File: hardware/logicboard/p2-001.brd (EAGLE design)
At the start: 72 x 72 mm, 49 parts, among them IC1 4066N, IC2 LTC485N, IC3 74LS07N, J1 LED, J2 RLY, J3 PWR, J4 DC9V, J5 Display, K1 G5V1, T1 2SC1815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

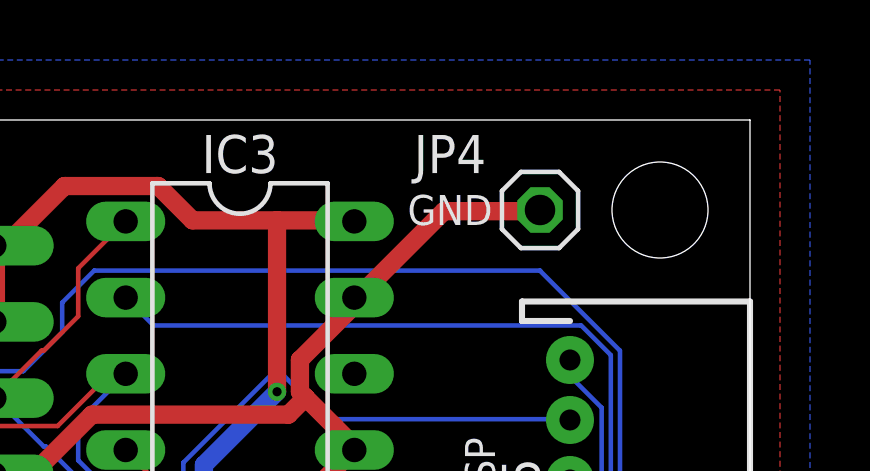
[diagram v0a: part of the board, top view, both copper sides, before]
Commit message: Renumbered number of jumpers.
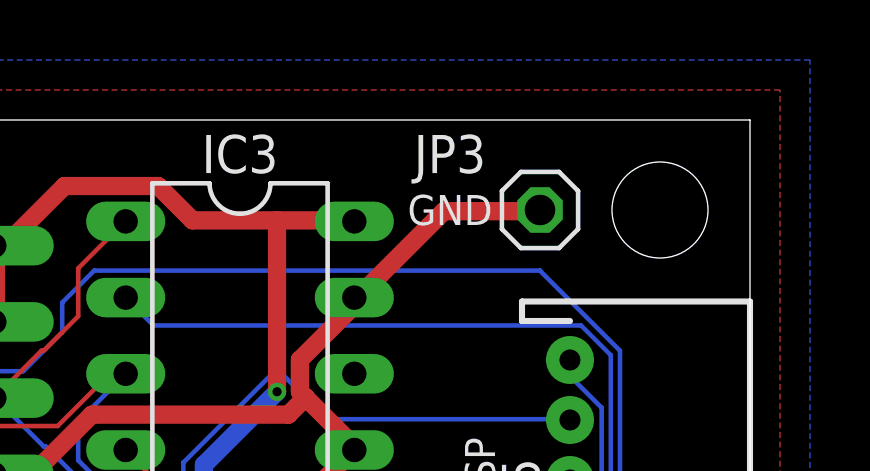
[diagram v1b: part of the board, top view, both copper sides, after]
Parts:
- renumbered JP4 to JP3
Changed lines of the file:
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@@
 <?xml version="1.0" encoding="utf-8"?>
 <!DOCTYPE eagle SYSTEM "eagle.dtd">
-<eagle version="9.5.2">
+<eagle version="9.6.1">
 <drawing>
 <settings>
@@
 <attribute name="VALUE" x="18" y="21" size="0.8128" layer="27" ratio="10" rot="R90" align="bottom-center"/>
 </element>
-<element name="JP4" library="pinhead" library_urn="urn:adsk.eagle:library:325" package="1X01" package3d_urn="urn:adsk.eagle:package:22485/2" value="GNDPIN" x="65" y="69" smashed="yes">
+<element name="JP3" library="pinhead" library_urn="urn:adsk.eagle:library:325" package="1X01" package3d_urn="urn:adsk.eagle:package:22485/2" value="GNDPIN" x="65" y="69" smashed="yes">
 <attribute name="NAME" x="62" y="71.5" size="1.27" layer="25" ratio="10" align="top-center"/>
 <attribute name="POPULARITY" value="64" x="65" y="69" size="1.778" layer="27" display="off"/>
@@
 <contactref element="IC2" pad="5"/>
 <contactref element="OK1" pad="5"/>
-<contactref element="JP4" pad="1"/>
+<contactref element="JP3" pad="1"/>
 <contactref element="C1" pad="2"/>
 <contactref element="C3" pad="2"/>

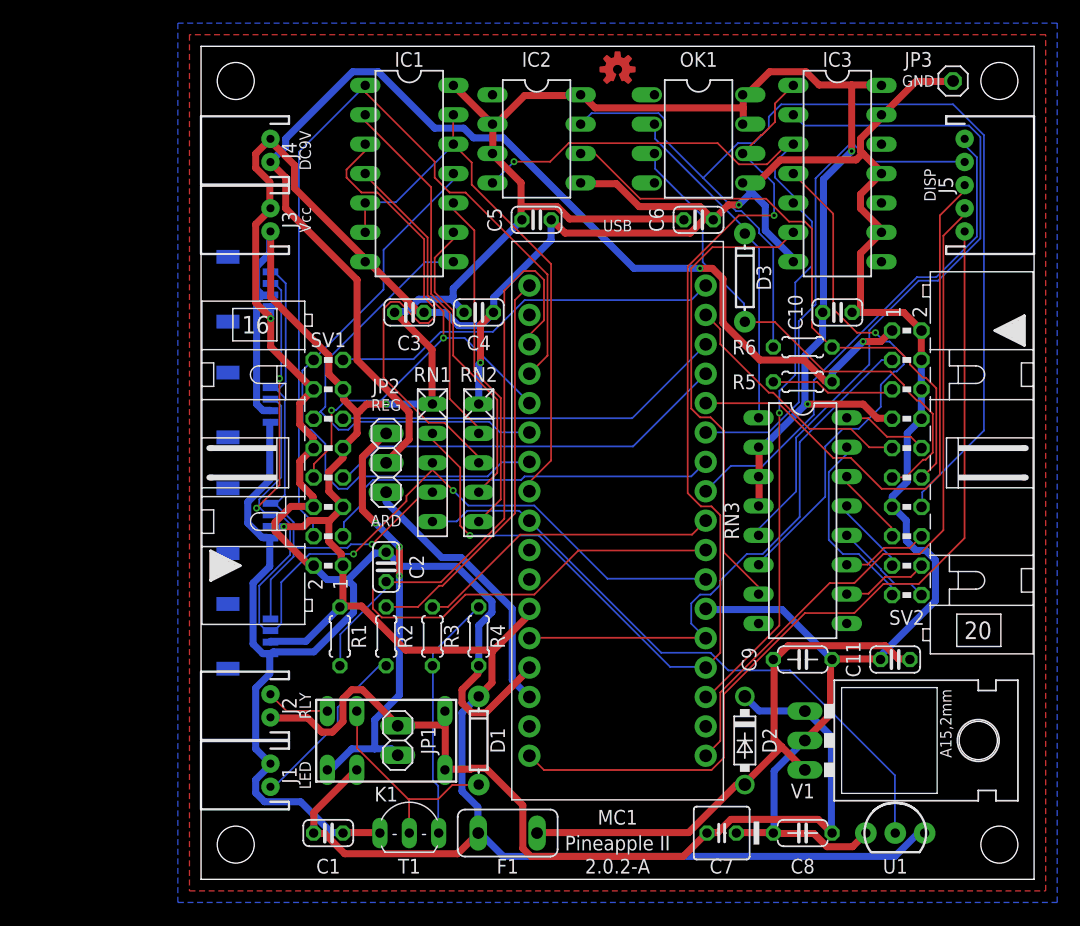
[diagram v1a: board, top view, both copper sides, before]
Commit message: Now Vcc is directly connected to the regulator.
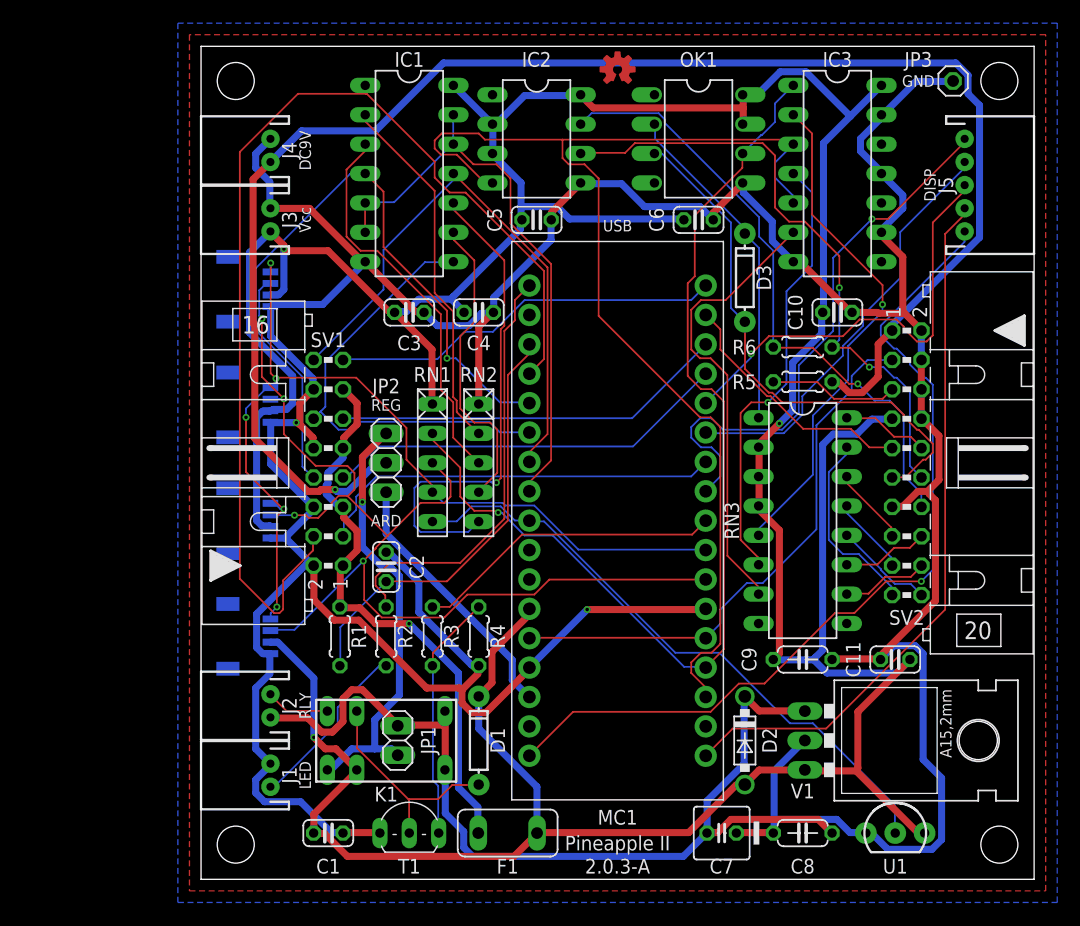
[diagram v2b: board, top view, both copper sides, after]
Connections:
- net +5V: now also F1.1, R1.2, SV1.1, SV1.13, SV1.5, SV1.9; no longer C11.1, C9.1, D2.A, F1.2, V1.OUT
- net VCC: now also C11.1, C9.1, D2.A, F1.2, V1.OUT; no longer F1.1, R1.2, SV1.1, SV1.13, SV1.5, SV1.9
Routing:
- net MTX-: track 94.7 -> 53.7 mm, vias 0 -> 1
- net VCC: track 317.0 -> 350.9 mm, vias 4 -> 3
- net +9V: track 104.8 -> 138.3 mm, vias 2 -> 1
- net ANLG1: track 74.8 -> 95.1 mm
- net TX: track 82.6 -> 102.2 mm, vias 2 -> 0
- net MTH: track 60.3 -> 44.0 mm, vias 0 -> 1
- net ANLG2: track 45.5 -> 60.7 mm, vias 2 -> 1
- net AREF: track 51.8 -> 37.6 mm
- net N$2: track 30.0 -> 43.1 mm, vias 0 -> 1
- net DISP3: track 49.7 -> 38.0 mm, vias 0 -> 1
- net ANLG2PDN: track 42.8 -> 33.8 mm
- net DISP2: track 43.8 -> 36.7 mm
- net MO1: track 45.1 -> 38.5 mm
- net DISP1: track 43.2 -> 48.7 mm, vias 0 -> 1
- net RX: track 95.8 -> 90.4 mm, vias 2 -> 1
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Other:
- board text added: "2.0.3-A"
- board text removed: "2.0.2-A"

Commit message: Changed resistance attached to LED.
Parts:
- R2: value 160 -> 120
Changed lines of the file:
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@@
 <?xml version="1.0" encoding="utf-8"?>
 <!DOCTYPE eagle SYSTEM "eagle.dtd">
-<eagle version="9.6.1">
+<eagle version="9.5.2">
 <drawing>
 <settings>
@@
 <attribute name="VALUE" x="69" y="60" size="0.8128" layer="27" ratio="20" rot="R90" align="bottom-center"/>
 </element>
-<element name="R2" library="resistor" library_urn="urn:adsk.eagle:library:348" package="0204/5" package3d_urn="urn:adsk.eagle:package:23488/1" value="160" x="16" y="21" smashed="yes" rot="R90">
+<element name="R2" library="resistor" library_urn="urn:adsk.eagle:library:348" package="0204/5" package3d_urn="urn:adsk.eagle:package:23488/1" value="120" x="16" y="21" smashed="yes" rot="R90">
 <attribute name="NAME" x="17" y="21" size="1.27" layer="25" ratio="10" rot="R90" align="top-center"/>
 <attribute name="VALUE" x="18" y="21" size="0.8128" layer="27" ratio="10" rot="R90" align="bottom-center"/>

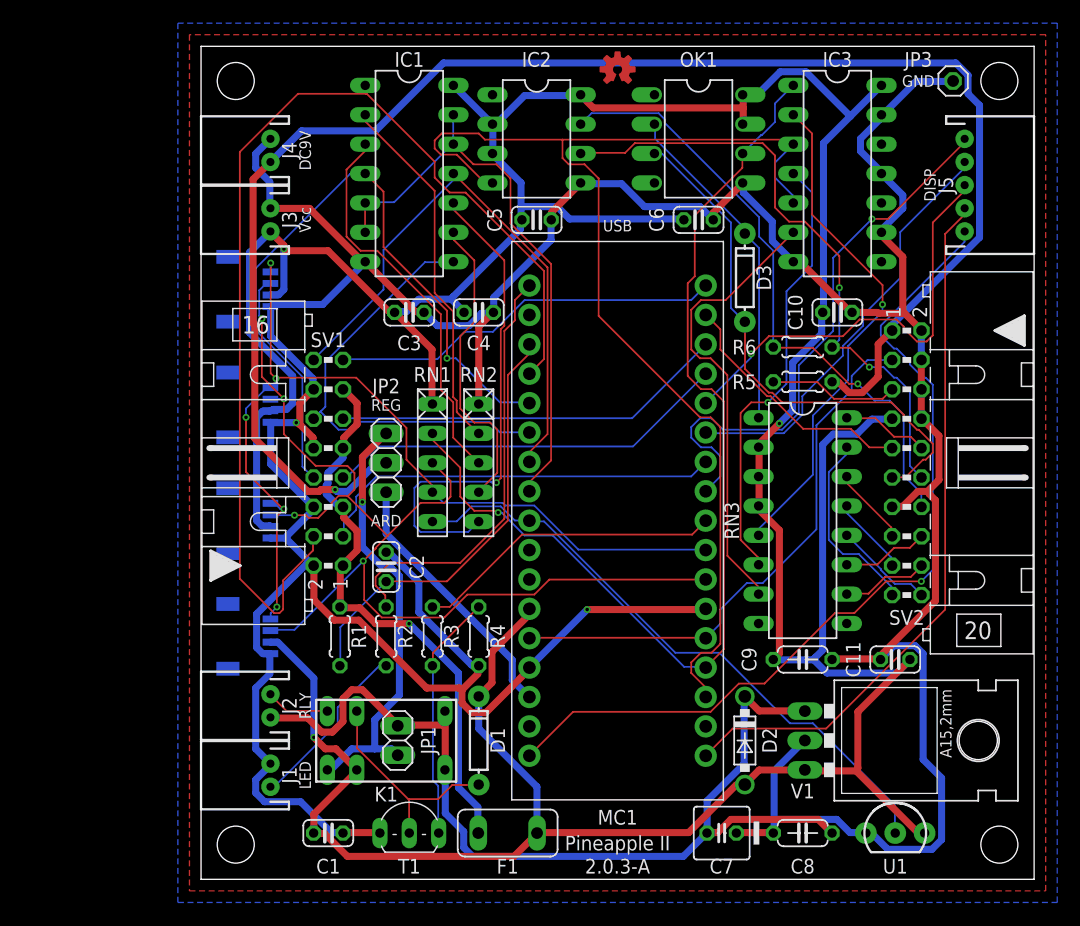
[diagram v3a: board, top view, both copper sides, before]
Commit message: Changed position of capacitors.
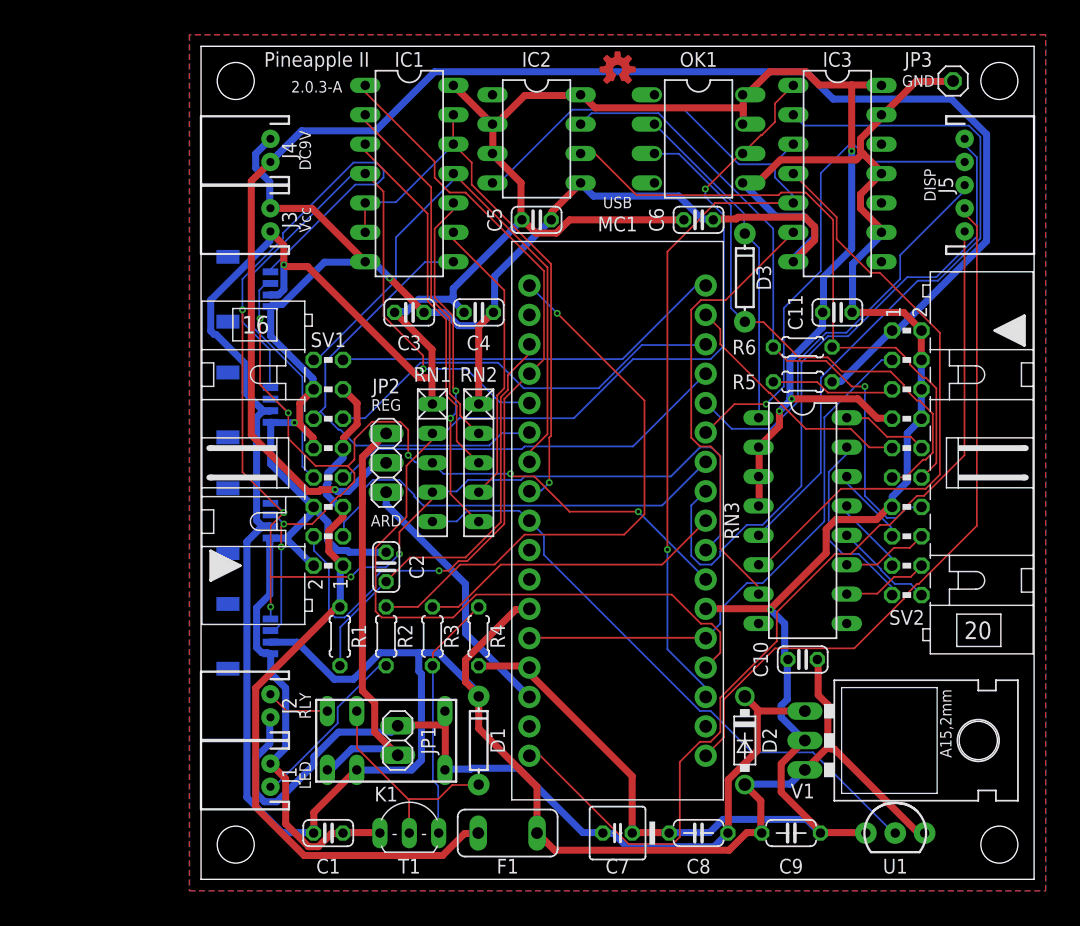
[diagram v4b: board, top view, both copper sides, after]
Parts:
- C10: value 10n -> 100n; device resistor:C025-024X044 -> rcl:C025-024X044
- C11: value 100n -> 10n; device rcl:C025-024X044 -> resistor:C025-024X044
- moved C11 30.4 mm to (55.0, 49.0), turned to 0 degrees
- moved C10 30.1 mm to (52.0, 19.0), turned to 180 degrees
- moved C9 15.0 mm to (51.0, 4.00)
- moved C7 9.00 mm to (36.0, 4.00)
- moved C8 9.00 mm to (43.0, 4.00)
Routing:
- net SCL: track 81.6 -> 125.4 mm
- net ANLG1: track 95.1 -> 72.8 mm, vias 0 -> 1
- net GND: track 353.3 -> 332.6 mm, vias 2 -> 3
- net RX: track 90.4 -> 107.9 mm
- net MTH: track 44.0 -> 60.4 mm, vias 1 -> 0
- net +5V: track 49.5 -> 64.6 mm, vias 1 -> 0
- net TX: track 102.2 -> 87.9 mm, vias 0 -> 1
- net N$2: track 43.1 -> 30.2 mm, vias 1 -> 2
- net SDA: track 96.9 -> 84.4 mm, vias 4 -> 7
- net LED0: track 37.3 -> 49.5 mm, vias 0 -> 1
- net MO1: track 38.5 -> 50.6 mm, vias 1 -> 0
- net DISP1: track 48.7 -> 58.2 mm, vias 1 -> 0
- net +9VB: track 86.0 -> 78.2 mm
- net DISP2: track 36.7 -> 42.2 mm, vias 0 -> 1
- net SCLK: track 75.9 -> 81.1 mm, vias 1 -> 0
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
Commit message: Designing.
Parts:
- added H1, H2: STAND-OFF, SparkFun-Hardware:STAND-OFF
- added JP4: (no value), pinhead:1X05
- moved LOGO1 53.7 mm to (-12.0, 46.0)
- moved R1 47.2 mm to (29.0, 65.0)
- moved C2 34.5 mm to (29.0, 59.0)
- moved C4 28.2 mm to (37.0, 24.0)
- moved C3 25.6 mm to (34.0, 29.0)
- moved R4 21.4 mm to (41.0, 8.00), turned to 0 degrees
- moved IC1 21.1 mm to (20.0, 40.0)
- moved R3 17.0 mm to (31.0, 8.00), turned to 0 degrees
- moved RN1 16.0 mm to (20.0, 20.0), turned to 0 degrees
- moved C5 13.9 mm to (16.0, 52.0)
- moved IC2 13.9 mm to (16.0, 59.0)
- moved R2 13.0 mm to (16.0, 8.00), turned to 0 degrees
- moved RN2 12.6 mm to (20.0, 24.0), turned to 0 degrees
- moved JP2 8.94 mm to (20.0, 28.0), turned to 0 degrees
- moved JP1 2.00 mm to (17.0, 14.0)
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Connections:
- net GND: now also JP4.2
- net SCL: now also JP4.4
- net SDA: now also JP4.5
- net VCC: now also JP4.1
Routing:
- net VCC: track 351.7 -> 0.00 mm, vias 4 -> 0
- net GND: track 332.6 -> 0.00 mm, vias 3 -> 0
- net +9V: track 134.1 -> 0.00 mm, vias 1 -> 0
- net SCL: track 125.4 -> 0.00 mm, vias 5 -> 0
- net RX: track 107.9 -> 0.00 mm, vias 1 -> 0
- net TX: track 87.9 -> 0.00 mm, vias 1 -> 0
- net SDA: track 84.4 -> 0.00 mm, vias 7 -> 0
- net SCLK: track 81.1 -> 0.00 mm
- net +9VB: track 78.2 -> 0.00 mm
- net ANLG1: track 72.8 -> 0.00 mm, vias 1 -> 0
- net +5V: track 64.6 -> 0.00 mm
- net ANLG2: track 62.4 -> 0.00 mm, vias 1 -> 0
- net MOSI: track 61.6 -> 0.00 mm
- net MTH: track 60.4 -> 0.00 mm
- net DISP1: track 58.2 -> 0.00 mm
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- removed copper zone on layer 1, net GND
- removed copper zone on layer 16, net GND

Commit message: Designing.
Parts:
- moved R5 17.3 mm to (35.0, 40.0)
- moved R6 16.0 mm to (36.0, 45.0)
- moved C11 1.00 mm to (55.0, 48.0)
- moved IC3 1.00 mm to (55.0, 59.0)

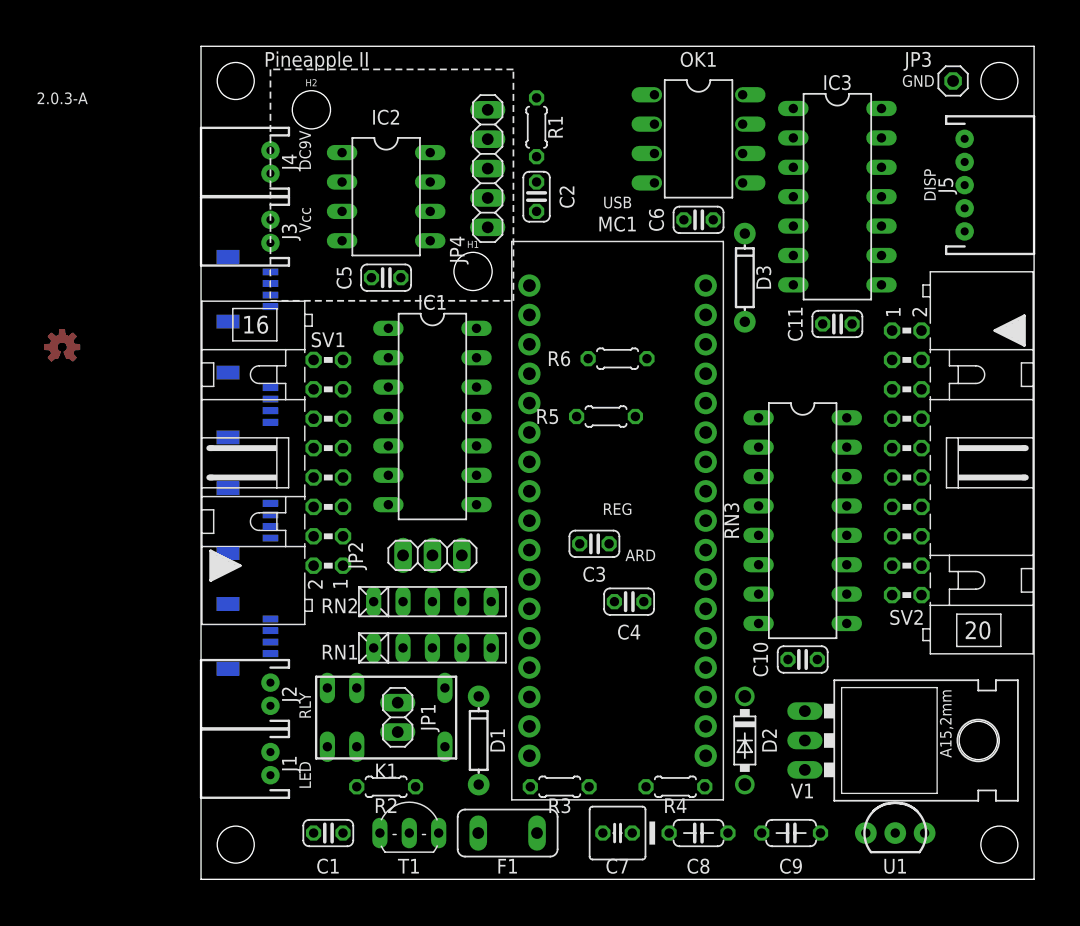
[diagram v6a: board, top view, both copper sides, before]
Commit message: Placed RTC board.
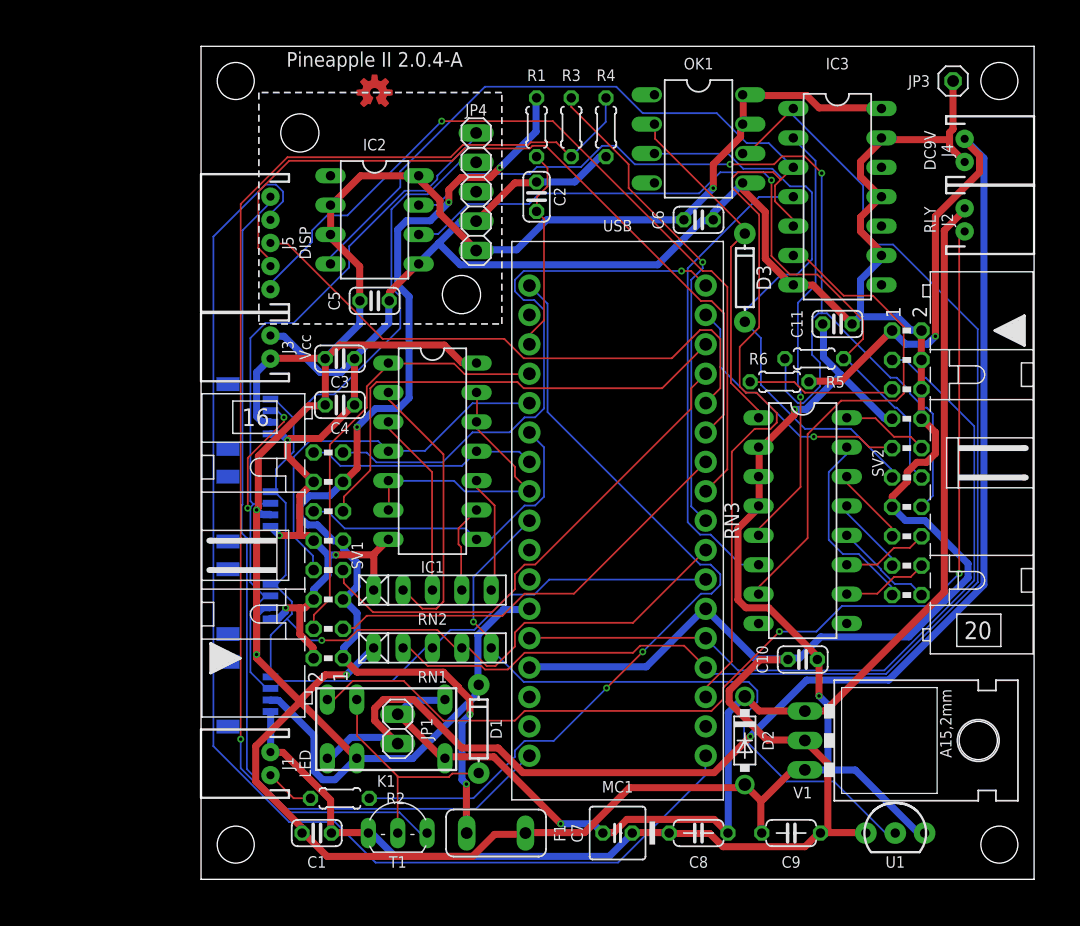
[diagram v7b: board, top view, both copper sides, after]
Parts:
- removed JP2: PWRSEL, pinhead:1X03
- moved J2 72.7 mm to (66.0, 57.0), turned to 270 degrees
- moved J5 60.2 mm to (6.00, 55.0), turned to 90 degrees
- moved J4 60.0 mm to (66.0, 63.0), turned to 270 degrees
- moved R4 57.3 mm to (35.0, 65.0), turned to 90 degrees
- moved R3 57.0 mm to (32.0, 65.0), turned to 90 degrees
- moved LOGO1 34.8 mm to (15.0, 68.0)
- moved C4 30.2 mm to (12.0, 41.0)
- moved C3 27.2 mm to (12.0, 45.0)
- moved R6 17.0 mm to (53.0, 45.0)
- moved R5 15.3 mm to (50.0, 43.0)
- moved JQ1 11.0 mm to (6.00, 40.0)
- moved J3 10.0 mm to (6.00, 46.0)
- moved JQ2 9.00 mm to (6.00, 32.0)
- moved SV1 8.00 mm to (11.0, 28.0)
- moved JQ3 7.00 mm to (6.00, 24.0)
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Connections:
- removed net +9VA: JP1.1, JP2.1, K1.1
- net +9V: now also JP1.1, K1.1; no longer JP2.2
- net VDD: no longer JP2.3
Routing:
- net GND: track 0.00 -> 336.9 mm, vias 0 -> 4
- net VCC: track 0.00 -> 327.8 mm, vias 0 -> 6
- net +9V: track 0.00 -> 145.2 mm, vias 0 -> 2
- net SDA: track 0.00 -> 115.5 mm, vias 0 -> 2
- net TX: track 0.00 -> 113.2 mm
- net RX: track 0.00 -> 109.9 mm
- net +9VB: track 0.00 -> 106.8 mm, vias 0 -> 1
- net MOSI: track 0.00 -> 106.6 mm
- net SCL: track 0.00 -> 105.2 mm, vias 0 -> 1
- net RLYDRV: track 0.00 -> 104.8 mm, vias 0 -> 1
- net RLYOUT: track 0.00 -> 92.3 mm, vias 0 -> 2
- net +5V: track 0.00 -> 91.8 mm, vias 0 -> 5
- net MTX-: track 0.00 -> 86.4 mm, vias 0 -> 2
- net SCLK: track 0.00 -> 78.4 mm
- net LED0: track 0.00 -> 71.5 mm, vias 0 -> 2
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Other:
- board text added: "Pineapple II 2.0.4-A"
- board text removed: "2.0.3-A"
- board text removed: "ARD"
- board text removed: "Pineapple II"
- board text removed: "REG"
